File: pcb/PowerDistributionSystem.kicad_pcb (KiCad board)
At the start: 4 copper layers, 50 x 50 mm, 87 parts, among them J1 Pin-Out, J2 JST-PH, J3 JST-PH, J4 JST-PH, J5 JST-PH, J6 JST-PH, U1 D24V7F5, U2 D24V7F3, U3 TMC2209-LA-T, U4 TMC2209-LA-T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

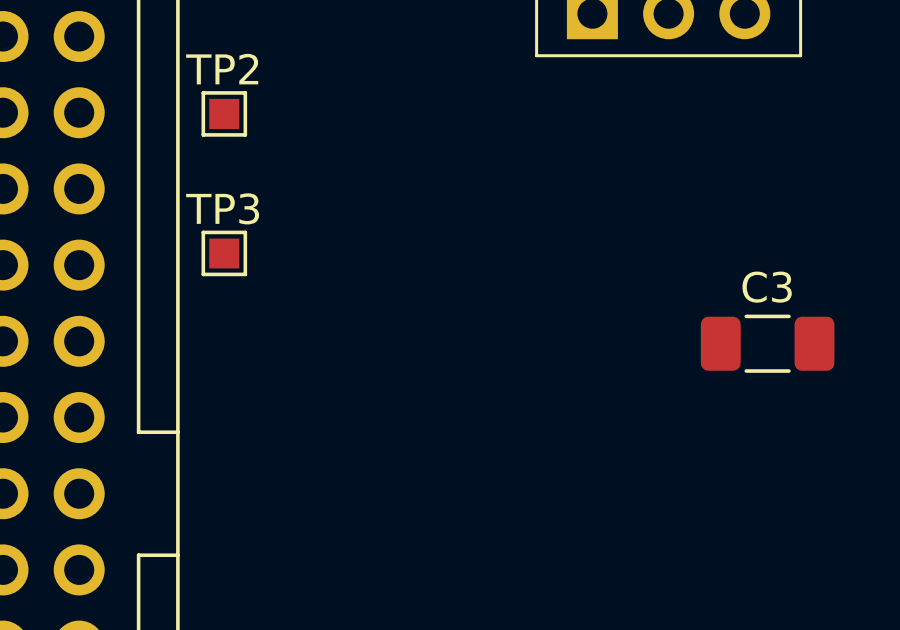
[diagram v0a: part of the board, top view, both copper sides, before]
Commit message: Added load switch.
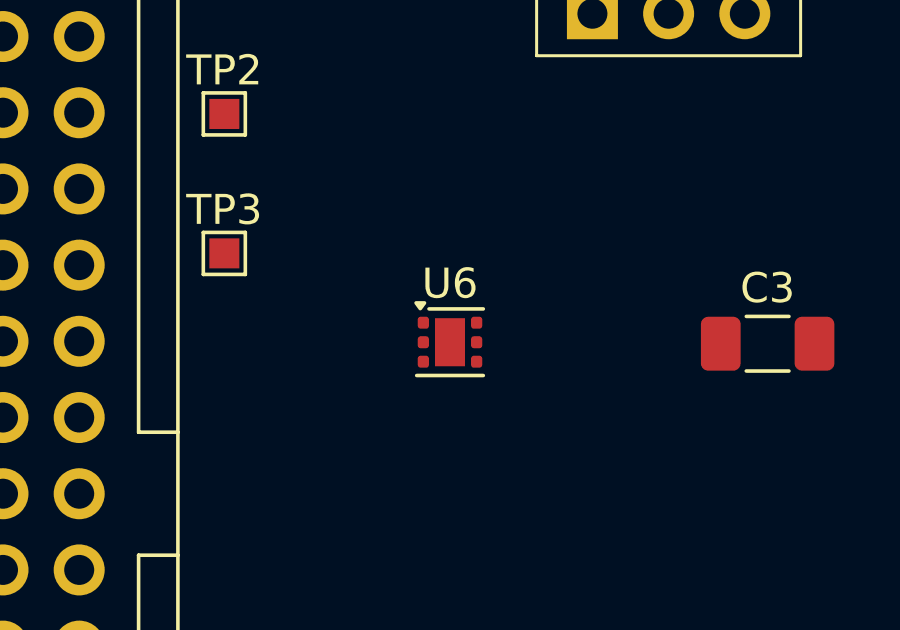
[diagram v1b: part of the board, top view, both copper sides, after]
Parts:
- added U6: TPS22810DRV, Package_SON:WSON-6-1EP_2x2mm_P0.65mm_EP1x1.6mm, F.Cu at (144.1, 94.3)
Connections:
- C10 pad 1: +BATT -> +MOTOR
- C14 pad 1: +BATT -> +MOTOR
- C15 pad 1: +BATT -> +MOTOR
- C16 pad 1: +BATT -> +MOTOR
- C18 pad 1: +BATT -> +MOTOR
- C2 pad 1: +BATT -> +MOTOR
- C22 pad 1: +BATT -> +MOTOR
- C23 pad 1: +BATT -> +MOTOR
- C24 pad 1: +BATT -> +MOTOR
- C6 pad 1: +BATT -> +MOTOR
- C7 pad 1: +BATT -> +MOTOR
- C8 pad 1: +BATT -> +MOTOR
- H10 pad MP: unconnected-(H10-PadMP) -> +PLUGGED_3.3V
- H11 pad MP: unconnected-(H11-PadMP) -> +5V
- H12 pad MP: unconnected-(H12-PadMP) -> +3.3V
- H5 pad MP: unconnected-(H5-PadMP) -> +PLUGGED_BATTERY
- H6 pad MP: unconnected-(H6-PadMP) -> +ENABLED_BATTERY
- H7 pad MP: unconnected-(H7-PadMP) -> +MOTOR
- H8 pad MP: unconnected-(H8-PadMP) -> BATTERY_ENABLE
- H9 pad MP: unconnected-(H9-PadMP) -> +PLUGGED_5V
- U1 pad VIN: unconnected-(U1-PadVIN) -> +PLUGGED_5V
- U1 pad VOUT: unconnected-(U1-PadVOUT) -> +5V
- U2 pad VIN: unconnected-(U2-PadVIN) -> +PLUGGED_3.3V
- U2 pad VOUT: unconnected-(U2-PadVOUT) -> +3.3V
- U3 pad 22: +BATT -> +MOTOR
- U3 pad 28: +BATT -> +MOTOR
- U4 pad 22: +BATT -> +MOTOR
- U4 pad 28: +BATT -> +MOTOR
- U5 pad 22: +BATT -> +MOTOR
- U5 pad 28: +BATT -> +MOTOR

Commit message: Fixed footprint of TMC2209-LA-T.
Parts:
- U3, U4, U5: footprint Package_DFN_QFN:VQFN-28-1EP_5x5mm_P0.5mm_EP3.7x3.7mm_ThermalVias -> pcb:VQFN-28-1EP_5x5mm_P0.5mm_EP3.7x3.7mm_ThermalVias
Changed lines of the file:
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@@
 		)
 	)
-	(footprint "Package_DFN_QFN:VQFN-28-1EP_5x5mm_P0.5mm_EP3.7x3.7mm_ThermalVias"
+	(footprint "pcb:VQFN-28-1EP_5x5mm_P0.5mm_EP3.7x3.7mm_ThermalVias"
 		(layer "F.Cu")
 		(at 199.65 90.51)
@@
 		)
 		(embedded_fonts no)
-		(model "${KICAD9_3DMODEL_DIR}/Package_DFN_QFN.3dshapes/VQFN-28-1EP_5x5mm_P0.5mm_EP3.7x3.7mm.step"
+		(model "${KIPRJMOD}/models/VQFN-28-1EP_5x5mm_P0.5mm_EP3.7x3.7mm.STEP"
 			(offset
 				(xyz 0 0 0)
@@
 			)
 			(rotate
-				(xyz 0 0 0)
+				(xyz -90 -0 -0)
 			)
 		)
@@
 		)
 	)
-	(footprint "Package_DFN_QFN:VQFN-28-1EP_5x5mm_P0.5mm_EP3.7x3.7mm_ThermalVias"
+	(footprint "pcb:VQFN-28-1EP_5x5mm_P0.5mm_EP3.7x3.7mm_ThermalVias"
 		(layer "F.Cu")
 		(at 163.8 100.46 -90)
@@
 		)
 		(embedded_fonts no)
-		(model "${KICAD9_3DMODEL_DIR}/Package_DFN_QFN.3dshapes/VQFN-28-1EP_5x5mm_P0.5mm_EP3.7x3.7mm.step"
+		(model "${KIPRJMOD}/models/VQFN-28-1EP_5x5mm_P0.5mm_EP3.7x3.7mm.STEP"
 			(offset
 				(xyz 0 0 0)
@@
 			)
 			(rotate
-				(xyz 0 0 0)
+				(xyz -90 -0 -0)
 			)
 		)
@@
 		(embedded_fonts no)
 	)
-	(footprint "Package_DFN_QFN:VQFN-28-1EP_5x5mm_P0.5mm_EP3.7x3.7mm_ThermalVias"
+	(footprint "pcb:VQFN-28-1EP_5x5mm_P0.5mm_EP3.7x3.7mm_ThermalVias"
 		(layer "F.Cu")
 		(at 199.65 116)
@@
 		)
 		(embedded_fonts no)
-		(model "${KICAD9_3DMODEL_DIR}/Package_DFN_QFN.3dshapes/VQFN-28-1EP_5x5mm_P0.5mm_EP3.7x3.7mm.step"
+		(model "${KIPRJMOD}/models/VQFN-28-1EP_5x5mm_P0.5mm_EP3.7x3.7mm.STEP"
 			(offset
 				(xyz 0 0 0)
@@
 			)
 			(rotate
-				(xyz 0 0 0)
+				(xyz -90 -0 -0)
 			)
 		)

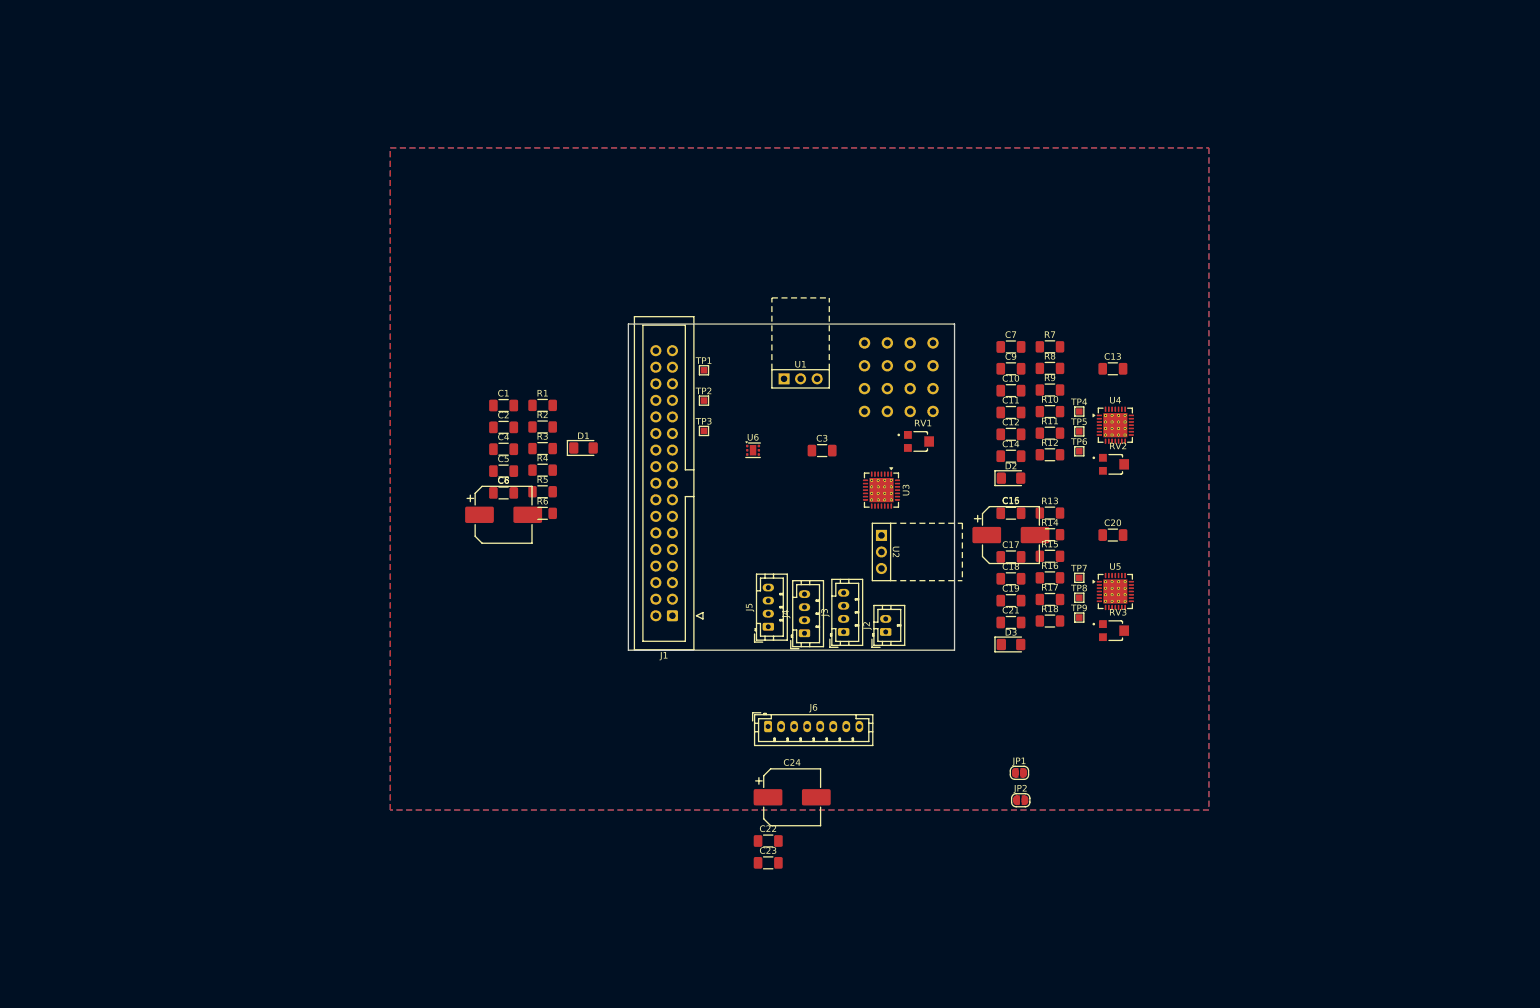
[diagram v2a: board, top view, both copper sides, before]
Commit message: Updated edge-cuts.
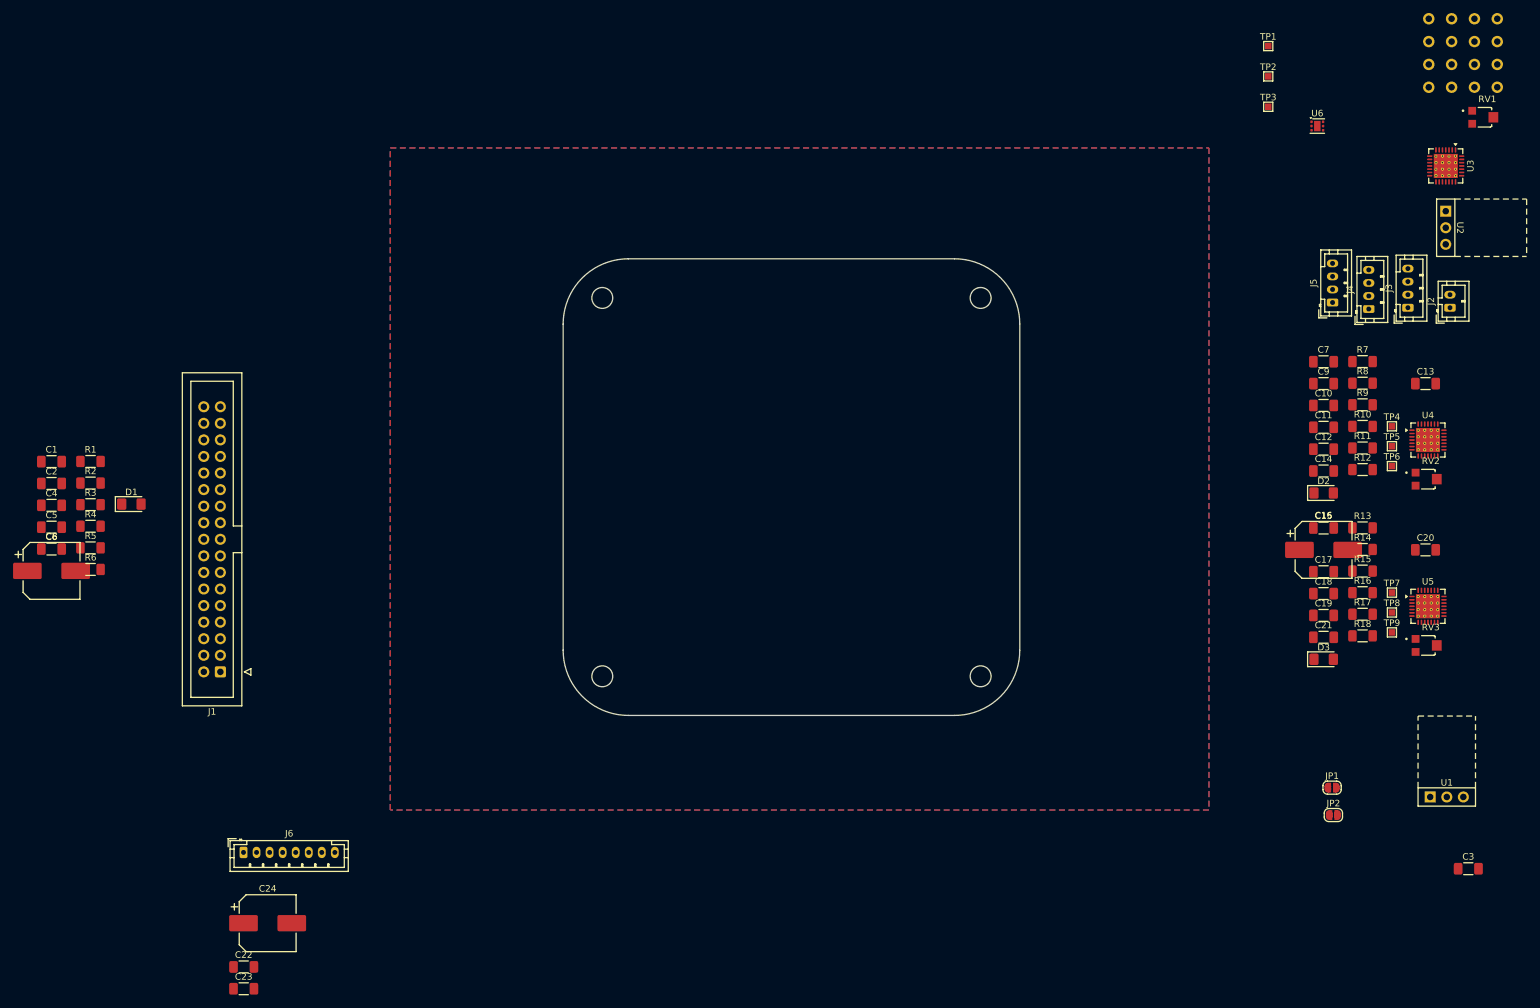
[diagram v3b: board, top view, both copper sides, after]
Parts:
- added H17: MountingHole, MountingHole:MountingHole_3.2mm_M3, F.Cu at (121.0, 71.0)
- added H18: MountingHole, MountingHole:MountingHole_3.2mm_M3, F.Cu at (179.0, 71.0)
- added H19: MountingHole, MountingHole:MountingHole_3.2mm_M3, F.Cu at (179.0, 129.0)
- added H20: MountingHole, MountingHole:MountingHole_3.2mm_M3, F.Cu at (121.0, 129.0)
- moved C3 118.0 mm to (253.8, 158.5)
- moved U1 118.0 mm to (250.5, 147.5)
- moved H1 99.8 mm to (247.7, 28.2)
- moved H10 99.8 mm to (254.7, 31.7)
- moved H11 99.8 mm to (254.7, 35.2)
- moved H12 99.8 mm to (254.7, 38.7)
- moved H13 99.8 mm to (258.2, 28.2)
- moved H14 99.8 mm to (258.2, 31.7)
- moved H15 99.8 mm to (258.2, 35.2)
- moved H16 99.8 mm to (258.2, 38.7)
- moved H2 99.8 mm to (247.7, 31.7)
- moved H3 99.8 mm to (247.7, 35.2)
- moved H4 99.8 mm to (247.7, 38.7)
- moved H5 99.8 mm to (251.2, 28.2)
- moved H6 99.8 mm to (251.2, 31.7)
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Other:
- board size 50 x 50 mm -> 70 x 70 mm

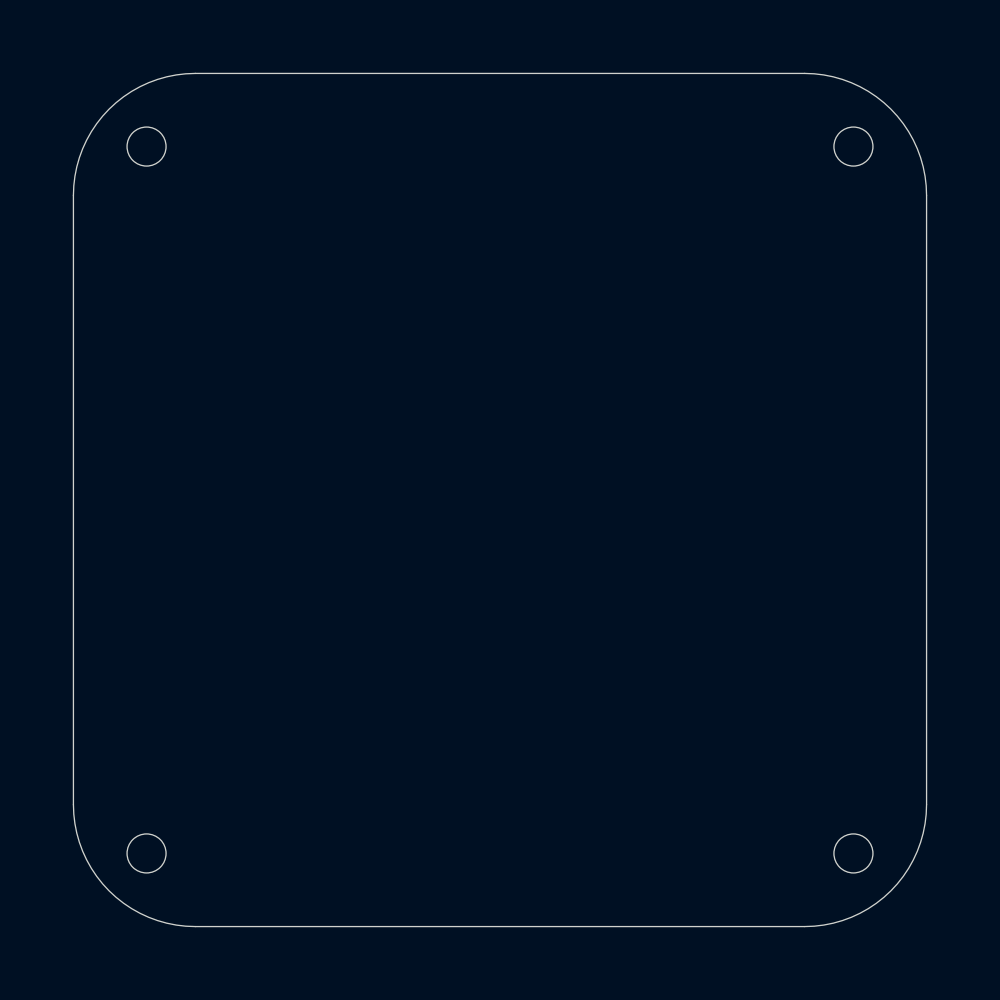
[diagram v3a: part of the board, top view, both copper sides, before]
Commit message: Updated CONSat model.
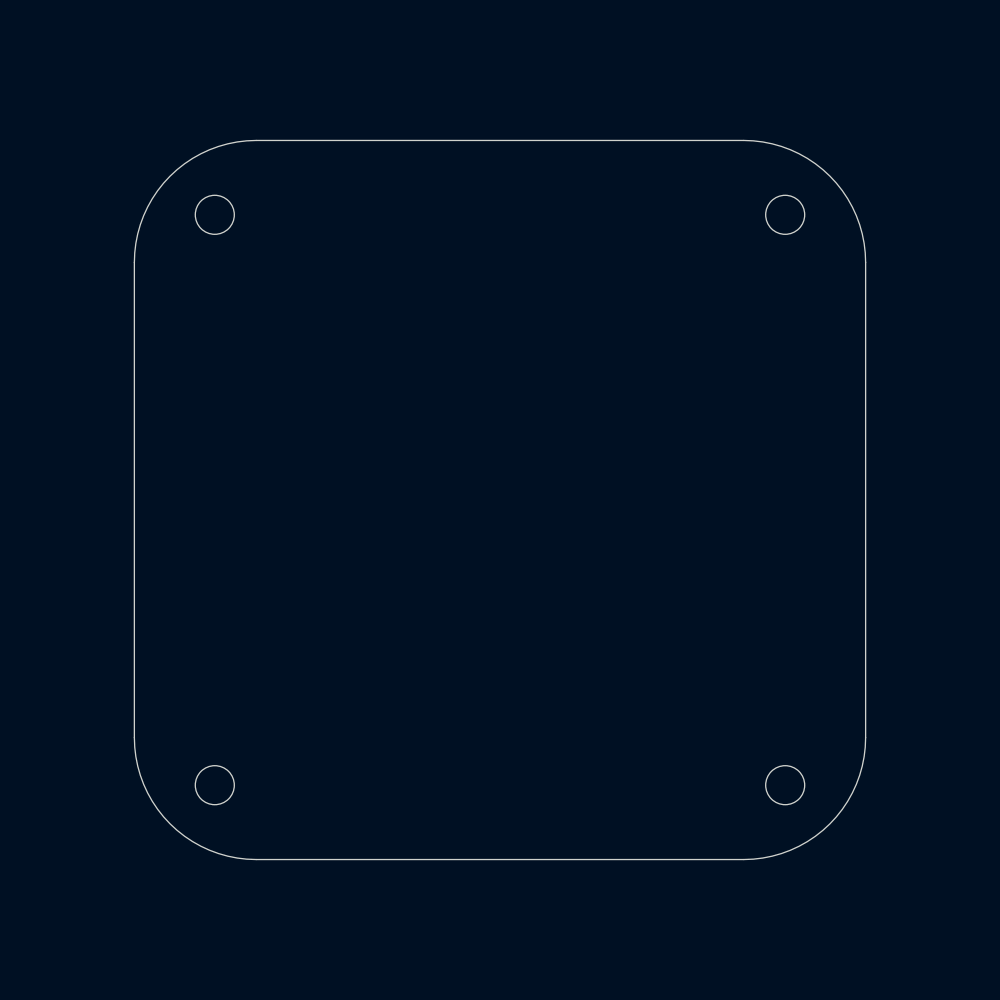
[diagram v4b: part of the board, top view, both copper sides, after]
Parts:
- moved H17 7.92 mm to (126.6, 76.6)
- moved H18 7.92 mm to (173.4, 76.6)
- moved H19 7.92 mm to (173.4, 123.4)
- moved H20 7.92 mm to (126.6, 123.4)
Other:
- board size 70 x 70 mm -> 60 x 59 mm
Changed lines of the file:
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@@
 		(embedded_fonts no)
 		(model "${KIPRJMOD}/models/CONSat.step"
-			(opacity 0.1700)
+			(opacity 0.2500)
 			(offset
-				(xyz 0 0 95)
+				(xyz 50 0 43)
 			)
 			(scale
@@
 			)
 			(rotate
-				(xyz -0 180 90)
+				(xyz -0 90 -0)
 			)
 		)
@@
 		(locked yes)
 		(layer "F.Cu")
-		(at 121 129)
+		(at 126.6 123.4)
 		(descr "Mounting Hole 3.2mm, M3, no annular, generated by kicad-footprint-generator mountinghole.py")
 		(tags "mountinghole M3")
@@
 		(locked yes)
 		(layer "F.Cu")
-		(at 179 71)
+		(at 173.4 76.6)
 		(descr "Mounting Hole 3.2mm, M3, no annular, generated by kicad-footprint-generator mountinghole.py")
 		(tags "mountinghole M3")
@@
 		(locked yes)
 		(layer "F.Cu")
-		(at 121 71)
+		(at 126.6 76.6)
 		(descr "Mounting Hole 3.2mm, M3, no annular, generated by kicad-footprint-generator mountinghole.py")
 		(tags "mountinghole M3")
@@
 		(locked yes)
 		(layer "F.Cu")
-		(at 179 129)
+		(at 173.4 123.4)
 		(descr "Mounting Hole 3.2mm, M3, no annular, generated by kicad-footprint-generator mountinghole.py")
 		(tags "mountinghole M3")
@@
 	)
 	(gr_line
-		(start 125 65)
-		(end 175 65)
+		(start 130 70.5)
+		(end 170 70.5)
 		(stroke
 			(width 0.05)
@@
 	)
 	(gr_line
-		(start 175 135)
-		(end 125 135)
+		(start 170 129.5)
+		(end 130 129.5)
 		(stroke
 			(width 0.05)
@@
 	)
 	(gr_line
-		(start 115 125)
-		(end 115 75)
+		(start 120 119.5)
+		(end 120 80.5)
 		(stroke
 			(width 0.05)
@@
 	)
 	(gr_arc
-		(start 115 75)
-		(mid 117.928932 67.928932)
-		(end 125 65)
+		(start 120 80.5)
+		(mid 122.928932 73.428932)
+		(end 130 70.5)
 		(stroke
 			(width 0.05)
@@
 	)
 	(gr_arc
-		(start 125 135)
-		(mid 117.928932 132.071068)
-		(end 115 125)
+		(start 130 129.5)
+		(mid 122.928932 126.571068)
+		(end 120 119.5)
 		(stroke
 			(width 0.05)
@@
 	)
 	(gr_arc
-		(start 175 65)
-		(mid 182.071068 67.928932)
-		(end 185 75)
+		(start 170 70.5)
+		(mid 177.071068 73.428932)
+		(end 180 80.5)
 		(stroke
 			(width 0.05)
@@
 	)
 	(gr_arc
-		(start 185 125)
-		(mid 182.071068 132.071068)
-		(end 175 135)
+		(start 180 119.5)
+		(mid 177.071068 126.571068)
+		(end 170 129.5)
 		(stroke
 			(width 0.05)
@@
 	)
 	(gr_line
-		(start 185 75)
-		(end 185 125)
+		(start 180 80.5)
+		(end 180 119.5)
 		(stroke
 			(width 0.05)
